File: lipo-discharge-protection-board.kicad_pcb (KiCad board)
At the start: 4 copper layers, 50 parts, among them J1 XT60, J2 2_PIN_SCREW, J3 Barrel_Jack, J4 Screw_Terminal_01x04, J5 Screw_Terminal_01x04, J6 Conn_02x02_Top_Bottom, J7 Conn_02x02_Top_Bottom, J8 Conn_02x04_Top_Bottom, Q1 AO3400A, Q2 AO3401A, Q3 AO3401A, Q4 AO3401A, Q5 AO3401A, U1 XL6009_module, U2 XL6009_module, U3 OPAMP

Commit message: Created pcb design
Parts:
- removed C11, C12: 10u 50V, Capacitor_SMD:C_1206_3216Metric_Pad1.33x1.80mm_HandSolder
- removed C13: 100n 50V, Capacitor_SMD:C_0805_2012Metric_Pad1.18x1.45mm_HandSolder
- removed J6, J7: Conn_02x02_Top_Bottom, Connector_Molex:Molex_Mini-Fit_Jr_5566-04A_2x02_P4.20mm_Vertical
- removed J8: Conn_02x04_Top_Bottom, Connector_Molex:Molex_Mini-Fit_Jr_5566-08A_2x04_P4.20mm_Vertical
- removed R17, R18, R19: 3k3, Capacitor_SMD:C_0805_2012Metric_Pad1.18x1.45mm_HandSolder
- removed U3: OPAMP, Package_SO:SOIC-8_3.9x4.9mm_P1.27mm
- added H1: MountingHole, MountingHole:MountingHole_3.2mm_M3, F.Cu at (96.0, 44.0)
- added H2: MountingHole, MountingHole:MountingHole_3.2mm_M3, F.Cu at (96.0, 96.0)
- added H3: MountingHole, MountingHole:MountingHole_3.2mm_M3, F.Cu at (13.0, 44.0)
- added H4: MountingHole, MountingHole:MountingHole_3.2mm_M3, F.Cu at (13.0, 96.0)
- C2, C8: value 100n 50V -> 10u 50V; footprint Capacitor_SMD:C_0805_2012Metric_Pad1.18x1.45mm_HandSolder -> Capacitor_SMD:C_1206_3216Metric_Pad1.33x1.80mm_HandSolder
- C3, C9: value 10u 50V -> 100n 50V; footprint Capacitor_SMD:C_1206_3216Metric_Pad1.33x1.80mm_HandSolder -> Capacitor_SMD:C_0805_2012Metric_Pad1.18x1.45mm_HandSolder
- J2: value 2_PIN_SCREW -> Barrel_Jack; footprint TerminalBlock:TerminalBlock_bornier-2_P5.08mm -> Connector_BarrelJack:BarrelJack_Horizontal
- J3: value Barrel_Jack -> 2_PIN_SCREW; footprint Connector_BarrelJack:BarrelJack_Horizontal -> TerminalBlock:TerminalBlock_bornier-2_P5.08mm
- J5: value Screw_Terminal_01x04 -> Conn_02x02_Top_Bottom; footprint TerminalBlock:TerminalBlock_bornier-4_P5.08mm -> Connector_Molex:Molex_Mini-Fit_Jr_5566-04A_2x02_P4.20mm_Vertical
- U2: value XL6009_module -> OPAMP; footprint misc_standard:XL6009_module_SMT -> Package_SO:SOIC-8_3.9x4.9mm_P1.27mm
- moved J4 255.4 mm to (4.00, 46.0), turned to 270 degrees
- moved J5 242.0 mm to (25.0, 61.0)
- moved C8 187.4 mm to (23.8, 46.0), turned to 270 degrees
- moved C10 185.4 mm to (28.8, 46.0), turned to 270 degrees
- moved U2 171.6 mm to (42.8, 75.5), turned to 180 degrees
- moved C9 164.7 mm to (49.5, 73.5), turned to 90 degrees
- moved C7 161.9 mm to (45.0, 50.0), turned to 270 degrees
- moved U1 148.8 mm to (50.0, 46.0), turned to 180 degrees
- moved R1 90.2 mm to (30.8, 92.8), turned to 270 degrees
- moved R5 90.1 mm to (51.0, 92.8), turned to 270 degrees
- moved C1 85.0 mm to (22.0, 71.5), turned to 270 degrees
- moved R12 84.0 mm to (36.0, 73.5), turned to 270 degrees
- moved R2 83.2 mm to (39.2, 92.8), turned to 270 degrees
- moved R10 79.6 mm to (79.8, 92.8), turned to 270 degrees
- moved J3 78.5 mm to (4.00, 89.8), turned to 270 degrees
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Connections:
- C2 pad 1: +VDC -> +BATT
- C3 pad 1: +BATT -> +VDC
- C4 pad 1: +VDC -> +BATT
- C5 pad 1: +BATT -> +VDC
- C7 pad 1: VCC2 -> VCC1
- C9 pad 1: VCC2 -> GND
- C9 pad 2: GND1 -> Net-(C9-Pad2)
- J3 pad 1: +BATT -> GND
- J3 pad 2: GND -> +BATT
- J4 pad 1: VCC2 -> VCC1
- J4 pad 2: VCC2 -> VCC1
- R13 pad 2: Net-(C13-Pad2) -> Net-(C9-Pad2)
- U1 pad 3: VCC2 -> VCC1
- U2 pad 1: +VDC -> Net-(R11-Pad1)
- U2 pad 2: GND -> Net-(D1-Pad1)
- U2 pad 3: VCC1 -> Net-(R14-Pad1)
- U2 pad 4: GND1 -> Net-(C9-Pad2)
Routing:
- net +BATT: track 0.00 -> 192.0 mm
- net VCC2: track 67.1 -> 0.00 mm
- net +VDC: track 0.00 -> 48.7 mm
- net Net-(R10-Pad1): track 0.00 -> 38.0 mm
- net Net-(D1-Pad1): track 0.00 -> 32.0 mm
- net Net-(R11-Pad2): track 0.00 -> 31.5 mm
- net Net-(Q1-Pad3): track 0.00 -> 29.5 mm
- net Net-(R11-Pad1): track 0.00 -> 25.1 mm
- net Net-(R6-Pad1): track 0.00 -> 23.1 mm
- net Net-(R5-Pad1): track 0.00 -> 19.5 mm
- net Net-(R14-Pad1): track 0.00 -> 14.3 mm
- net Net-(R2-Pad1): track 0.00 -> 11.7 mm
- net Net-(C9-Pad2): track 0.00 -> 10.4 mm
- net Net-(R1-Pad1): track 0.00 -> 7.93 mm
- net VCC1: track 79.5 -> 73.3 mm
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- added copper zone on B.Cu, net GND
- added copper zone on F.Cu, net GND
- added copper zone on B.Cu, net GND1
- added copper zone on F.Cu, net GND1
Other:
- board outline added: 100 x 60 mm
- board text added: "2S"
- board text added: "3S"
- board text added: "CUSTOM CUTOUT VOLTAGE SET"
- board text added: "RV1"

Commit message: Updated bad footprints and exported bom
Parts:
- moved C1 40.0 mm to (22.0, 31.5)
- moved C10 40.0 mm to (28.8, 6.00)
- moved C2 40.0 mm to (26.0, 32.0)
- moved C3 40.0 mm to (90.2, 31.0)
- moved C4 40.0 mm to (30.2, 32.0)
- moved C5 40.0 mm to (89.5, 34.8)
- moved C6 40.0 mm to (89.5, 38.8)
- moved C7 40.0 mm to (45.0, 9.96)
- moved C8 40.0 mm to (23.8, 6.00)
- moved C9 40.0 mm to (49.5, 33.5)
- moved D1 40.0 mm to (58.2, 40.8)
- moved H1 40.0 mm to (96.0, 4.00)
- moved H2 40.0 mm to (96.0, 56.0)
- moved H3 40.0 mm to (13.0, 4.00)
- moved H4 40.0 mm to (13.0, 56.0)
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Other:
- board text added: "!! ONLY SHORT ONE SET OF JUMPERS !!"
- board text added: "DC IN"
- board text added: "DC OUT"
- board text added: "GND"
- board text added: "POT"
- board text added: "SVE JE TO RESEARCH AND DEVELOPMENT! - Vesnaa"
- board text added: "V+"
- board text removed: "RV1"

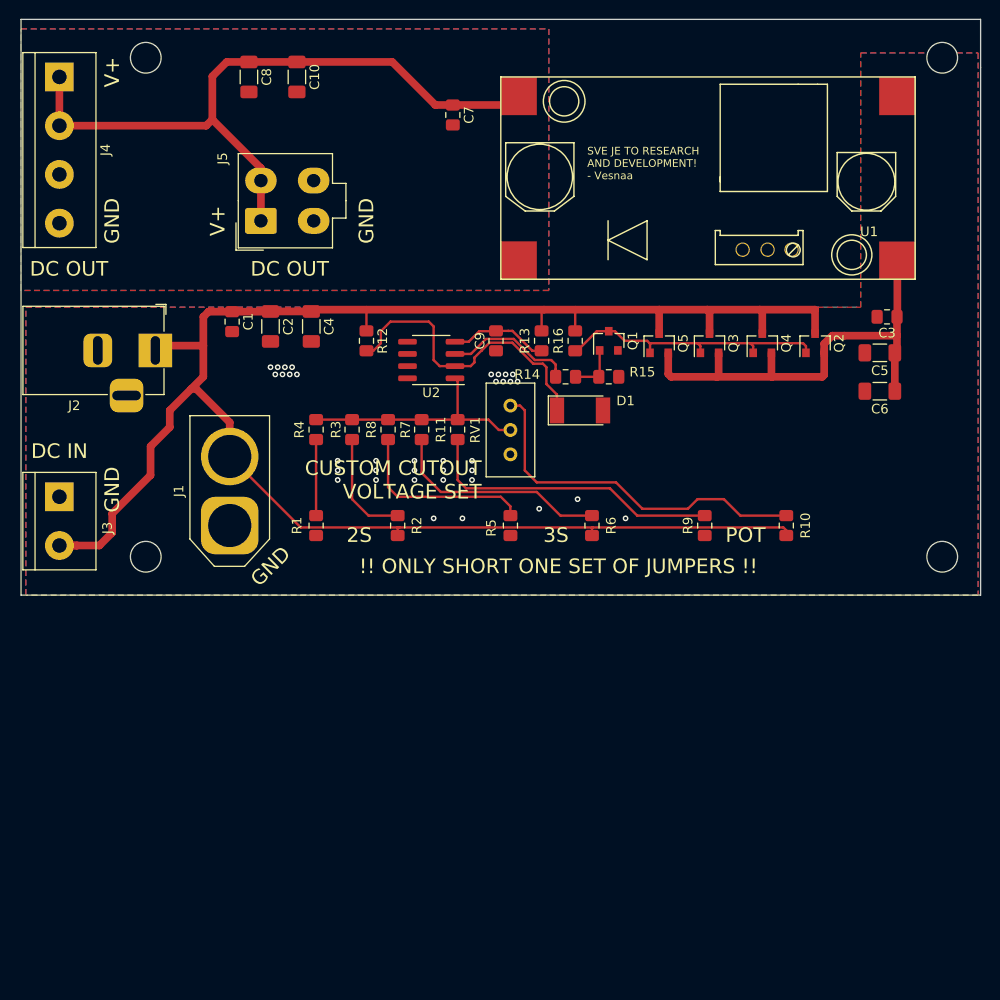
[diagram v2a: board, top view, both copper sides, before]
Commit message: Added alarm circuit
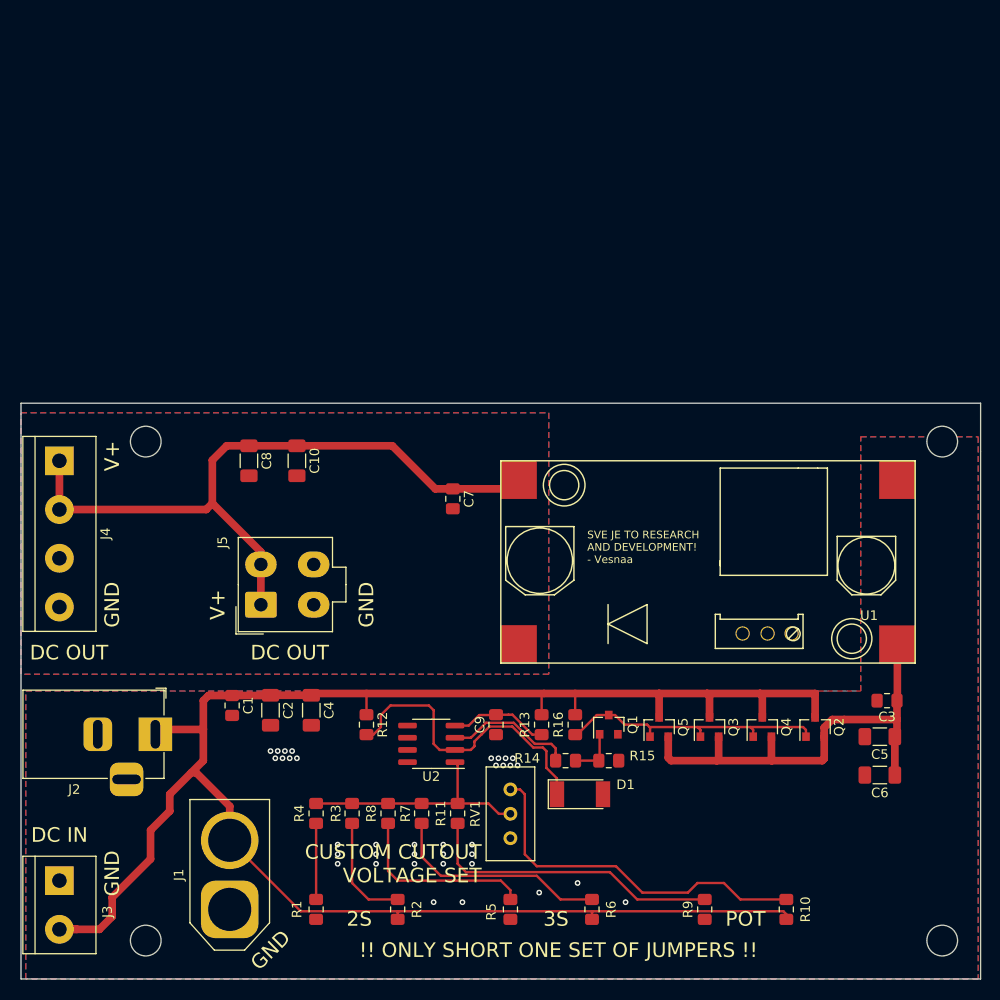
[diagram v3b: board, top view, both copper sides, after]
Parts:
- moved C1 40.0 mm to (22.0, 71.5)
- moved C10 40.0 mm to (28.8, 46.0)
- moved C2 40.0 mm to (26.0, 72.0)
- moved C3 40.0 mm to (90.2, 71.0)
- moved C4 40.0 mm to (30.2, 72.0)
- moved C5 40.0 mm to (89.5, 74.8)
- moved C6 40.0 mm to (89.5, 78.8)
- moved C7 40.0 mm to (45.0, 50.0)
- moved C8 40.0 mm to (23.8, 46.0)
- moved C9 40.0 mm to (49.5, 73.5)
- moved D1 40.0 mm to (58.2, 80.8)
- moved H1 40.0 mm to (96.0, 44.0)
- moved H2 40.0 mm to (96.0, 96.0)
- moved H3 40.0 mm to (13.0, 44.0)
- moved H4 40.0 mm to (13.0, 96.0)
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
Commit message: Added components for the alarm circuit and fixed wrong footprints
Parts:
- added C11: 100n 50V, Capacitor_SMD:C_0805_2012Metric_Pad1.18x1.45mm_HandSolder, F.Cu at (-39.0, 59.4)
- added D2: LED, LED_SMD:LED_0805_2012Metric_Pad1.15x1.40mm_HandSolder, F.Cu at (0.65, 46.0)
- added R17: 2k2, Resistor_SMD:R_0805_2012Metric_Pad1.20x1.40mm_HandSolder, F.Cu at (-34.2, 59.3)
- added R18: 47R, Resistor_SMD:R_0805_2012Metric_Pad1.20x1.40mm_HandSolder, F.Cu at (-19.4, 48.3)
- added R19: 220R, Resistor_SMD:R_0805_2012Metric_Pad1.20x1.40mm_HandSolder, F.Cu at (-19.4, 51.3)
- added R20: 330R, Resistor_SMD:R_0805_2012Metric_Pad1.20x1.40mm_HandSolder, F.Cu at (-20.6, 54.8)
- added RV2: 10k, Potentiometer_THT:Potentiometer_Bourns_3296W_Vertical, F.Cu at (-33.3, 50.1)
- added U3: OPAMP, Package_SO:SOIC-8_3.9x4.9mm_P1.27mm, F.Cu at (-26.0, 50.1)
- added U4: L7805, Package_TO_SOT_SMD:SOT-89-3_Handsoldering, F.Cu at (-27.0, 56.3)
- added U5: EL3H7, lipo-discharge-protection-board:SOIC127P700X210-4N, F.Cu at (-35.9, 55.6)
- R1, R10, R11, R12, R13, R14, R15, R16, R2, R3, R4, R5, R6, R7, R8, R9: footprint Capacitor_SMD:C_0805_2012Metric_Pad1.18x1.45mm_HandSolder -> Resistor_SMD:R_0805_2012Metric_Pad1.20x1.40mm_HandSolder

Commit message: Updated PCB
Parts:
- removed the C11 at (-39.0, 59.4)
- removed D2: LED, LED_SMD:LED_0805_2012Metric_Pad1.15x1.40mm_HandSolder
- removed the RV2 at (-33.3, 50.1)
- added ALARM: LED, LED_SMD:LED_0805_2012Metric_Pad1.15x1.40mm_HandSolder, F.Cu at (88.8, 92.0)
- added C10: 100n 50V, Capacitor_SMD:C_0805_2012Metric_Pad1.18x1.45mm_HandSolder, F.Cu at (75.0, 81.0)
- added J6: Conn_01x02_Male, Connector_PinHeader_1.27mm:PinHeader_1x02_P1.27mm_Vertical, F.Cu at (97.8, 88.8)
- added Q1: AO3400A, Package_TO_SOT_SMD:SOT-23, F.Cu at (81.8, 84.2)
- added Q3: AO3401A, Package_TO_SOT_SMD:SOT-23, F.Cu at (81.8, 80.2)
- added R16: 3k3, Resistor_SMD:R_0805_2012Metric_Pad1.20x1.40mm_HandSolder, F.Cu at (75.2, 84.0)
- added R17: 1k, Resistor_SMD:R_0805_2012Metric_Pad1.20x1.40mm_HandSolder, F.Cu at (77.2, 87.8)
- added R23: 330R, Resistor_SMD:R_0805_2012Metric_Pad1.20x1.40mm_HandSolder, F.Cu at (93.0, 83.6)
- added RV1: 10k, Potentiometer_THT:Potentiometer_Bourns_3296W_Vertical, F.Cu at (56.8, 85.8)
- R20: value 330R -> 3k3
- moved U5 132.8 mm to (95.2, 76.8), turned to 270 degrees
- moved U4 118.2 mm to (87.8, 84.3), turned to 180 degrees
- moved R22 110.6 mm to (83.8, 91.0), turned to 270 degrees
- moved R9 110.1 mm to (72.2, 87.5), turned to 180 degrees
- moved U2 100.7 mm to (69.0, 83.5), turned to 180 degrees
- moved R20 100.0 mm to (76.5, 78.8)
- moved R13 89.9 mm to (65.5, 77.8), turned to 270 degrees
- renumbered C3 to C1, C9 to C11, C1 to C2, C5 to C3, C2 to C4, C6 to C5, C4 to C6, C10 to C9, Q1 to Q2, Q2 to Q4, Q3 to Q5, Q4 to Q6, Q5 to Q7, R9 to R10, R10 to R11, R11 to R12, R18 to R13, R12 to R14, R13 to R15, R14 to R18, R15 to R19, R16 to R21, R19 to R22, R17 to R9, RV1 to RV2, U3 to U2, U2 to U3
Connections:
- R20 pad 1: Net-(R20-Pad1) -> +VDC
- R20 pad 2: Net-(D2-Pad2) -> Net-(Q1-Pad3)
- U2 pad 3: Net-(U3-Pad3) -> Net-(R16-Pad1)
- U4 pad 1: Net-(U3-Pad3) -> Net-(Q3-Pad2)
- U5 pad 1: Net-(R20-Pad1) -> Net-(R23-Pad1)
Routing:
- net +BATT: track 192.0 -> 223.2 mm
- net Net-(D1-Pad1): track 32.0 -> 54.2 mm
- net Net-(R9-Pad1): track 0.00 -> 19.0 mm
- net Net-(D2-Pad2): track 0.00 -> 14.2 mm
- net Net-(J6-Pad2): track 0.00 -> 12.3 mm
- net Net-(Q3-Pad2): track 0.00 -> 11.3 mm
- net Net-(C10-Pad2): track 0.00 -> 11.0 mm
- net Net-(R23-Pad1): track 0.00 -> 10.6 mm
- net Net-(J6-Pad1): track 0.00 -> 10.2 mm
- net Net-(Q1-Pad3): track 0.00 -> 8.02 mm
- net Net-(Q1-Pad1): track 0.00 -> 7.92 mm
- net +VDC: track 48.7 -> 56.2 mm
- net Net-(D2-Pad1): track 0.00 -> 3.97 mm
- net Net-(R16-Pad1): track 0.00 -> 3.83 mm
- net GND1: vias 0 -> 8
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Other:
- board text added: "ALARM VOLTAGE SET"
- board text added: "ALARM_C"
- board text added: "ALARM_C ALARM_E"
- board text removed: "2S"
